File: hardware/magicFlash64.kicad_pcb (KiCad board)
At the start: 2 copper layers, 43.8 x 50.8 mm, 29 parts, among them J1 1x5, J2 1x7, J3 1x3, J4 1x4, J5 AVR ISP, U1 ROMSOCKET, U2 ATMEGA48-20PU, U3 AM29F040, U4 74LS138

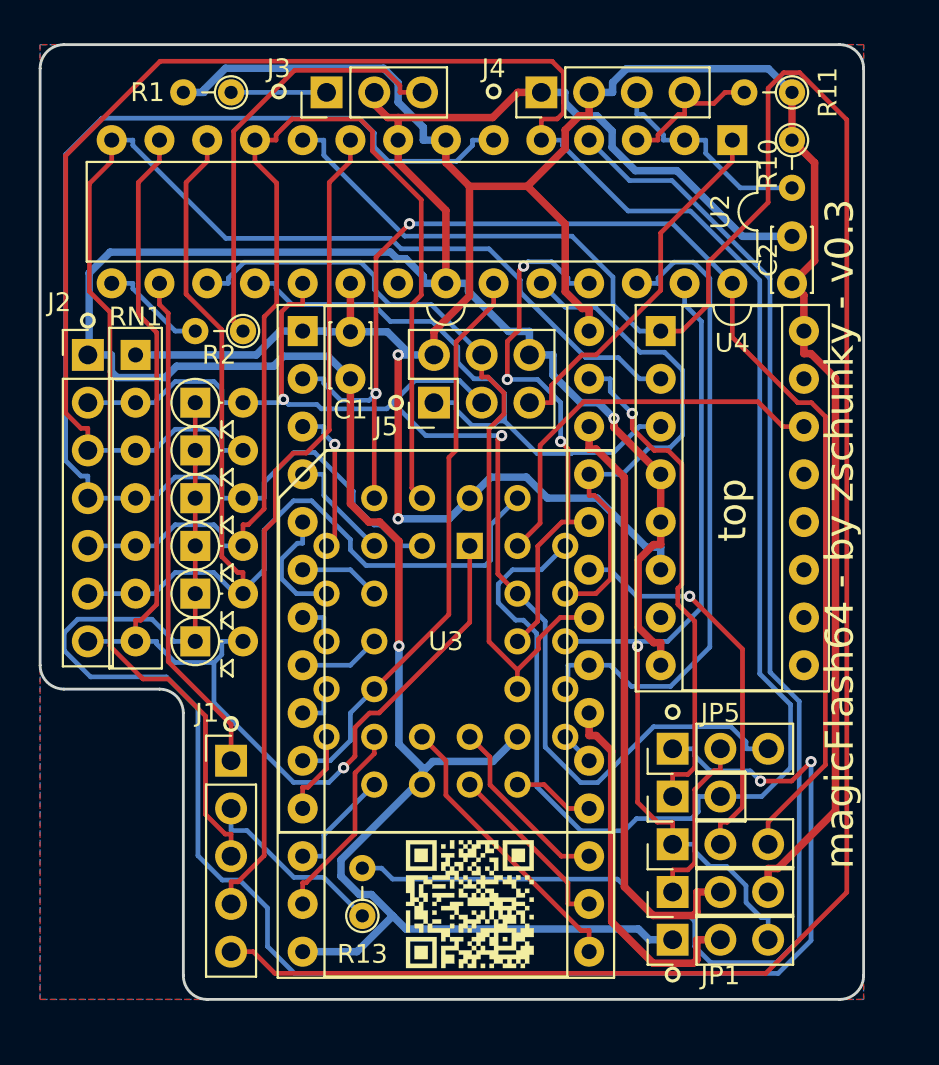
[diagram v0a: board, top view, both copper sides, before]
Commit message: Added PCB v0.3 SMD 1206
SMD (partially) version of v0.3 board
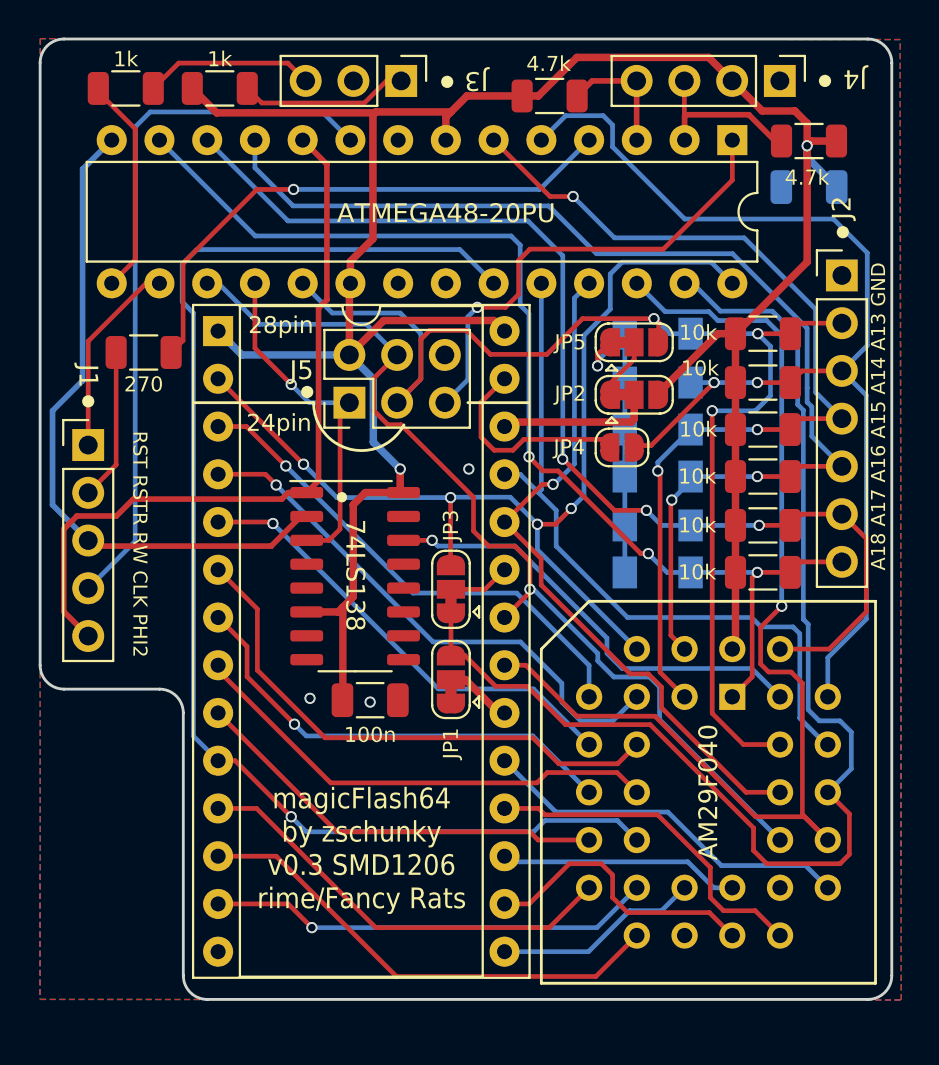
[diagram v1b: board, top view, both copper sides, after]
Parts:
- removed G***: LOGO, zschunkyFootprints:qrcode
- removed RN1: 10k, Resistors_THT:R_Array_SIP7
- added R3: 10k, Resistor_SMD:R_1206_3216Metric, F.Cu at (117.2, 73.8)
- added R4: 10k, Resistor_SMD:R_1206_3216Metric, F.Cu at (117.2, 76.4)
- added R5: 10k, Resistor_SMD:R_1206_3216Metric, F.Cu at (117.2, 78.9)
- added R6: 10k, Resistor_SMD:R_1206_3216Metric, F.Cu at (117.2, 81.4)
- added R7: 10k, Resistor_SMD:R_1206_3216Metric, F.Cu at (117.2, 84.0)
- added R8: 10k, Resistor_SMD:R_1206_3216Metric, F.Cu at (117.2, 86.5)
- C1: footprint Capacitors_THT:C_Disc_D3.4mm_W2.1mm_P2.50mm -> Capacitor_SMD:C_1206_3216Metric; moved to B.Cu
- C2: footprint Capacitors_THT:C_Disc_D3.4mm_W2.1mm_P2.50mm -> Capacitor_SMD:C_1206_3216Metric
- D1, D2, D3, D4, D5, D6: footprint Diodes_THT:D_DO-35_SOD27_P2.54mm_Vertical_AnodeUp -> Diode_SMD:D_MiniMELF; moved to B.Cu
- JP1, JP2, JP3, JP5: footprint Pin_Headers:Pin_Header_Straight_1x03_Pitch2.54mm -> Jumper:SolderJumper-3_P1.3mm_Bridged12_RoundedPad1.0x1.5mm
- JP4: footprint Pin_Headers:Pin_Header_Straight_1x02_Pitch2.54mm -> Jumper:SolderJumper-2_P1.3mm_Open_RoundedPad1.0x1.5mm
- R1, R13, R2: footprint Resistors_THT:R_Axial_DIN0204_L3.6mm_D1.6mm_P2.54mm_Vertical -> Resistor_SMD:R_1206_3216Metric
- R10, R11: value 4.7K -> 4.7k; footprint Resistors_THT:R_Axial_DIN0204_L3.6mm_D1.6mm_P2.54mm_Vertical -> Resistor_SMD:R_1206_3216Metric
- U4: footprint Housings_DIP:DIP-16_W7.62mm_Socket -> Package_SO:SO-16_3.9x9.9mm_P1.27mm
- moved J2 40.3 mm to (121.4, 70.7)
- moved R13 32.2 mm to (84.2, 74.8), turned to 0 degrees
- moved C2 31.6 mm to (96.3, 93.3), turned to 0 degrees
- moved JP2 26.5 mm to (110.3, 77.0), turned to 0 degrees
- moved C1 26.4 mm to (119.7, 66.0), turned to 0 degrees
- moved D4 24.9 mm to (111.6, 81.4)
- moved D1 24.9 mm to (111.6, 73.8)
- moved D6 24.9 mm to (111.6, 86.5)
- moved D3 24.9 mm to (111.6, 78.9)
- moved D5 24.9 mm to (111.6, 84.0)
- moved D2 24.9 mm to (111.6, 76.4)
- moved JP5 21.7 mm to (110.3, 74.3), turned to 0 degrees
- moved U4 20.8 mm to (95.5, 86.7)
- moved JP4 18.8 mm to (109.7, 79.8), turned to 0 degrees
- moved J1 18.4 mm to (81.3, 79.7)
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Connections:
- U2 pad 21: (no net) -> unconnected-(U2-Pad21)
- U4 pad 10: (no net) -> unconnected-(U4-Pad10)
- U4 pad 11: (no net) -> unconnected-(U4-Pad11)
- U4 pad 12: (no net) -> unconnected-(U4-Pad12)
- U4 pad 13: (no net) -> unconnected-(U4-Pad13)
- U4 pad 15: (no net) -> unconnected-(U4-Pad15)
- U4 pad 7: (no net) -> unconnected-(U4-Pad7)
- U4 pad 9: (no net) -> unconnected-(U4-Pad9)
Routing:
- net GND: track 168.1 -> 0.00 mm, vias 2 -> 3
- net PHI2: track 122.2 -> 39.7 mm
- net LOROM: track 93.0 -> 16.5 mm, vias 2 -> 1
- net SEL_A14: track 133.6 -> 60.6 mm, vias 0 -> 2
- net RESTORE: track 75.1 -> 29.3 mm, vias 0 -> 1
- net RW: track 77.7 -> 35.8 mm
- net A0: track 30.5 -> 69.4 mm, vias 0 -> 1
- net A10: track 34.7 -> 59.4 mm, vias 0 -> 1
- net A4: track 4.34 -> 28.9 mm
- net A13_VCC: track 32.4 -> 8.36 mm
- net A6: track 6.05 -> 28.8 mm, vias 0 -> 1
- net VCC: track 154.1 -> 131.6 mm
- net A3: track 2.46 -> 24.5 mm, vias 0 -> 1
- net A2: track 4.34 -> 25.7 mm
- net A11: track 46.3 -> 66.5 mm, vias 1 -> 0
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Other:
- board size 43.8 x 50.8 mm -> 45.3 x 51.1 mm
- net class Default removed
- net class pwr removed
- rule pad_to_mask_clearance: 0.2 -> 0
- board text added: "A18 A17 A16 A15 A14 A13 GND"
- board text added: "RST RSTR RW CLK PHI2"
- board text added: "magicFlash64 by zschunky v0.3 SMD1206 rime/Fancy Rats"
- board text removed: "magicFlash64 - by zschunky - v0.3"
- board text removed: "top"
- board text removed: "°"
